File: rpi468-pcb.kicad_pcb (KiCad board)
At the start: 2 copper layers, 14 x 28.3 mm, 11 parts, among them J1 USB_A, J2 USB_C_Receptacle_USB2.0, J3 Conn_01x04_Female, U1 LM397

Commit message: updated pcb
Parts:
- removed R1: 5.1k, Resistor_SMD:R_0603_1608Metric_Pad0.98x0.95mm_HandSolder
- J3: footprint Connector_PinHeader_1.00mm:PinHeader_1x04_P1.00mm_Vertical -> Connector_JST:JST_SH_BM04B-SRSS-TB_1x04-1MP_P1.00mm_Vertical
- moved J3 2.04 mm to (167.9, 117.4), turned to 0 degrees
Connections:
- J2 pad B5: Net-(J2-PadB5) -> Net-(J2-PadA5)
- J3 pad 2: Net-(J3-Pad2) -> Net-(S1-Pad4)
- J3 pad 3: Net-(J3-Pad3) -> Net-(S1-Pad6)
- R2 pad 1: Net-(J2-PadB5) -> Net-(J2-PadA5)
- S1 pad 4: Net-(J3-Pad3) -> Net-(S1-Pad4)
- S1 pad 6: Net-(J3-Pad2) -> Net-(S1-Pad6)
- U1 pad 1: Net-(J2-PadB5) -> Net-(J2-PadA5)
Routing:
- net Net-(J2-PadB5): track 42.0 -> 0.00 mm, vias 4 -> 0
- net Net-(J2-PadA5): track 11.1 -> 48.3 mm, vias 2 -> 5
- net Net-(S1-Pad6): track 0.00 -> 13.0 mm
- net Net-(J3-Pad2): track 11.5 -> 0.00 mm
- net Net-(S1-Pad4): track 0.00 -> 9.86 mm
- net Net-(J3-Pad3): track 8.37 -> 0.00 mm, vias 2 -> 0
- net +5V: track 45.6 -> 50.0 mm
- net Net-(R5-Pad2): track 25.5 -> 21.5 mm
- net Net-(J1-Pad2): track 17.9 -> 20.1 mm
- net Net-(J1-Pad3): track 14.2 -> 16.2 mm
- net GND: track 45.1 -> 43.9 mm
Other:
- board size 14 x 28.3 mm -> 14 x 29.8 mm

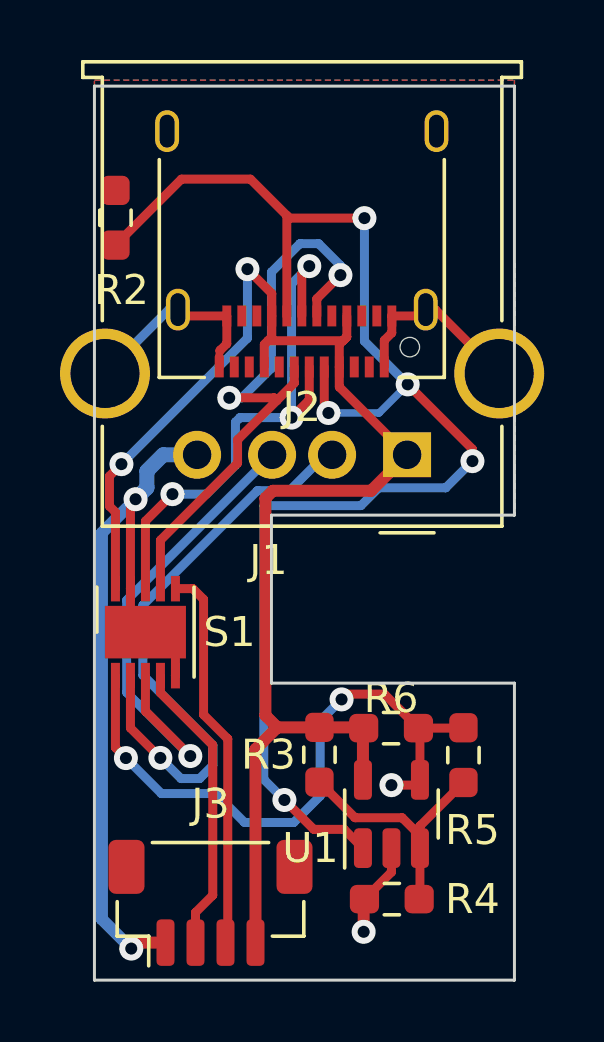
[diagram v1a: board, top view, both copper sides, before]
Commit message: updated cut outline
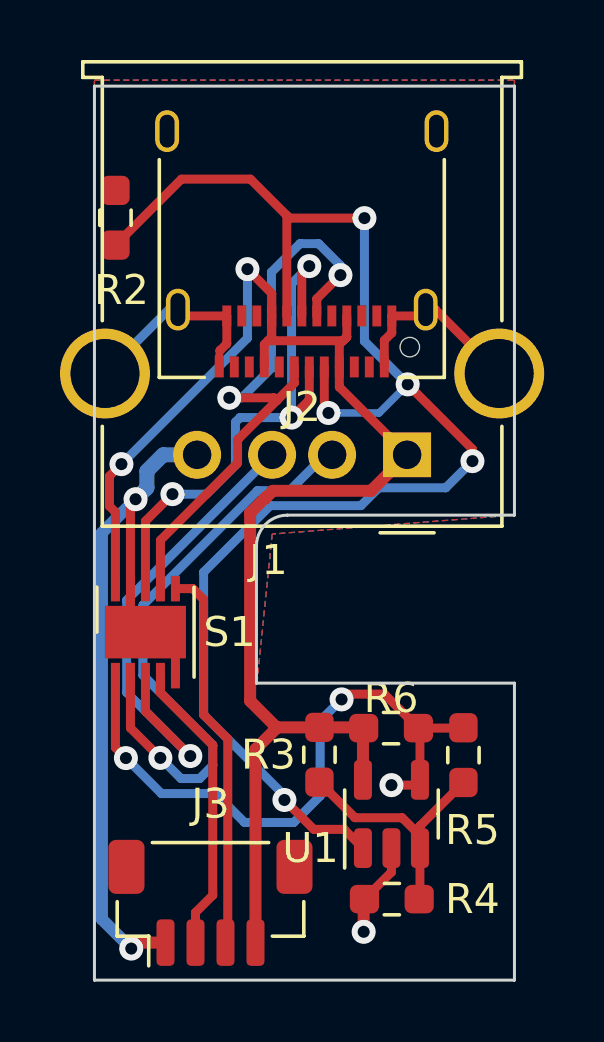
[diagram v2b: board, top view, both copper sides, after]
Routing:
- net Net-(J2-PadA5): track 48.3 -> 49.8 mm
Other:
- outline, holes or cut-outs redrawn
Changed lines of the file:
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@@
     )
     (pad_to_mask_clearance 0)
-    (grid_origin 166.116 102.5906)
+    (grid_origin 175.768 107.1626)
     (pcbplotparams
       (layerselection 0x00010fc_ffffffff)
@@
     )
   )
+  (gr_line (start 170.434 104.5) (end 178 104.5) (layer "Edge.Cuts") (width 0.1))
+  (gr_line (start 169.4 110.1) (end 169.4 105.537051) (layer "Edge.Cuts") (width 0.1))
   (gr_line (start 178 110.1) (end 178 120) (layer "Edge.Cuts") (width 0.1))
   (gr_line (start 178 90.2) (end 178 104.5) (layer "Edge.Cuts") (width 0.1))
-  (gr_line (start 169.9 104.5) (end 169.9 110.1) (layer "Edge.Cuts") (width 0.1))
-  (gr_line (start 169.9 110.1) (end 178 110.1) (layer "Edge.Cuts") (width 0.1))
+  (gr_line (start 169.4 110.1) (end 178 110.1) (layer "Edge.Cuts") (width 0.1))
   (gr_line (start 178 90.2) (end 164 90.2) (layer "Edge.Cuts") (width 0.1))
   (gr_line (start 178 120) (end 164 120) (layer "Edge.Cuts") (width 0.1))
   (gr_line (start 164 120) (end 164 90.2) (layer "Edge.Cuts") (width 0.1))
-  (gr_line (start 178 104.5) (end 169.9 104.5) (layer "Edge.Cuts") (width 0.1))
+  (gr_arc (start 169.4 105.537051) (mid 169.70222 104.804377) (end 170.434 104.5) (layer "Edge.Cuts") (width 0.1))
   (segment (start 169.785896 98.685896) (end 169.911792 98.56) (width 0.3) (layer "F.Cu") (net 1))
   (segment (start 169.785896 98.685896) (end 172.285896 98.685896) (width 0.3) (layer "F.Cu") (net 1))
   (segment (start 164.5 103.2) (end 164.9 102.8) (width 0.3) (layer "F.Cu") (net 1))
   (segment (start 173.2218 103.689) (end 169.9452 103.689) (width 0.4) (layer "F.Cu") (net 1))
+  (segment (start 169.7 103.9342) (end 169.682957 103.9342) (width 0.4) (layer "F.Cu") (net 1))
+  (segment (start 169.682957 103.9342) (end 169.1894 104.427757) (width 0.4) (layer "F.Cu") (net 1))
   (segment (start 174.4218 102.489) (end 174.3718 102.489) (width 0.4) (layer "F.Cu") (net 1))
   (segment (start 172.411792 98.56) (end 172.411792 97.86) (width 0.3) (layer "F.Cu") (net 1))
   (segment (start 169.661792 99.56) (end 169.661792 98.81) (width 0.3) (layer "F.Cu") (net 1))
+  (segment (start 169.1894 110.6932) (end 170.0712 111.575) (width 0.4) (layer "F.Cu") (net 1))
   (segment (start 169.7 103.9342) (end 169.9452 103.689) (width 0.4) (layer "F.Cu") (net 1))
   (segment (start 172.95 111.625) (end 172.975 111.6) (width 0.4) (layer "F.Cu") (net 1))
@@
   (segment (start 169.661792 98.81) (end 169.785896 98.685896) (width 0.3) (layer "F.Cu") (net 1))
   (segment (start 169.1 96.3) (end 169.911792 97.111792) (width 0.3) (layer "F.Cu") (net 1))
-  (segment (start 169.7 111.1784) (end 169.7 103.9342) (width 0.4) (layer "F.Cu") (net 1))
+  (segment (start 169.1894 104.427757) (end 169.1894 110.6932) (width 0.4) (layer "F.Cu") (net 1))
   (segment (start 169.3686 118.7492) (end 169.3686 112.303) (width 0.4) (layer "F.Cu") (net 1))
   (segment (start 164.5 104.2) (end 164.5 103.2) (width 0.3) (layer "F.Cu") (net 1))
-  (segment (start 170.0966 111.575) (end 169.7 111.1784) (width 0.4) (layer "F.Cu") (net 1))
   (segment (start 170.0966 111.575) (end 171.5 111.575) (width 0.4) (layer "F.Cu") (net 1))
+  (segment (start 170.0712 111.575) (end 170.0966 111.575) (width 0.4) (layer "F.Cu") (net 1))
   (segment (start 164.7 106.95) (end 164.7 104.4) (width 0.3) (layer "F.Cu") (net 1))
   (segment (start 172.161792 99.56) (end 172.161792 98.81) (width 0.3) (layer "F.Cu") (net 1))
@@
   (via (at 173 94.6) (size 0.8) (drill 0.4) (layers "F.Cu" "B.Cu") (net 8))
   (via (at 176.6 102.7) (size 0.8) (drill 0.4) (layers "F.Cu" "B.Cu") (net 8))
-  (segment (start 172.882999 104.1828) (end 169.6466 104.1828) (width 0.3) (layer "B.Cu") (net 8))
+  (segment (start 167.64 111.154494) (end 170.3324 113.846894) (width 0.3) (layer "B.Cu") (net 8))
+  (segment (start 175.711 103.589) (end 173.476799 103.589) (width 0.3) (layer "B.Cu") (net 8))
   (segment (start 174.440923 100.140923) (end 173 98.7) (width 0.3) (layer "B.Cu") (net 8))
   (segment (start 174.440923 100.140923) (end 173.486998 101.094848) (width 0.25) (layer "B.Cu") (net 8))
   (segment (start 173.486998 101.094848) (end 171.799548 101.094848) (width 0.25) (layer "B.Cu") (net 8))
+  (segment (start 167.64 106.4006) (end 167.64 111.154494) (width 0.3) (layer "B.Cu") (net 8))
   (segment (start 173 98.7) (end 173 94.6) (width 0.3) (layer "B.Cu") (net 8))
-  (segment (start 169.6466 104.1828) (end 169.6466 113.3094) (width 0.3) (layer "B.Cu") (net 8))
   (segment (start 176.6 102.7) (end 175.711 103.589) (width 0.3) (layer "B.Cu") (net 8))
-  (segment (start 169.6466 113.3094) (end 170.3324 113.9952) (width 0.3) (layer "B.Cu") (net 8))
-  (segment (start 175.711 103.589) (end 173.476799 103.589) (width 0.3) (layer "B.Cu") (net 8))
   (segment (start 173.476799 103.589) (end 172.882999 104.1828) (width 0.3) (layer "B.Cu") (net 8))
+  (segment (start 172.882999 104.1828) (end 169.8578 104.1828) (width 0.3) (layer "B.Cu") (net 8))
+  (segment (start 170.3324 113.846894) (end 170.3324 113.9952) (width 0.3) (layer "B.Cu") (net 8))
+  (segment (start 169.8578 104.1828) (end 167.64 106.4006) (width 0.3) (layer "B.Cu") (net 8))
   (segment (start 167.3686 118.7492) (end 167.3686 117.7464) (width 0.3) (layer "F.Cu") (net 10))
   (segment (start 166.2 109.85) (end 166.2 110.4216) (width 0.3) (layer "F.Cu") (net 10))
@@
       (pts
         (xy 178.0032 104.4956)
-        (xy 169.9006 104.4956)
-        (xy 169.9006 110.0836)
+        (xy 169.926 105.1306)
+        (xy 169.418 110.0836)
         (xy 178 110.109)
         (xy 178.0032 119.9896)
@@
       (pts
         (xy 178.0286 104.4956)
-        (xy 169.9006 104.4956)
-        (xy 169.9006 110.0836)
+        (xy 169.926 105.1306)
+        (xy 169.418 110.0836)
         (xy 177.9778 110.109)
         (xy 178 119.9896)
